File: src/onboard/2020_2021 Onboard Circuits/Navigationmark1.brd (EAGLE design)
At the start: 63.2 x 68.6 mm, 44 parts, among them IC1 A5975D, IC2 A5975D, IC3 CD74AC257M96

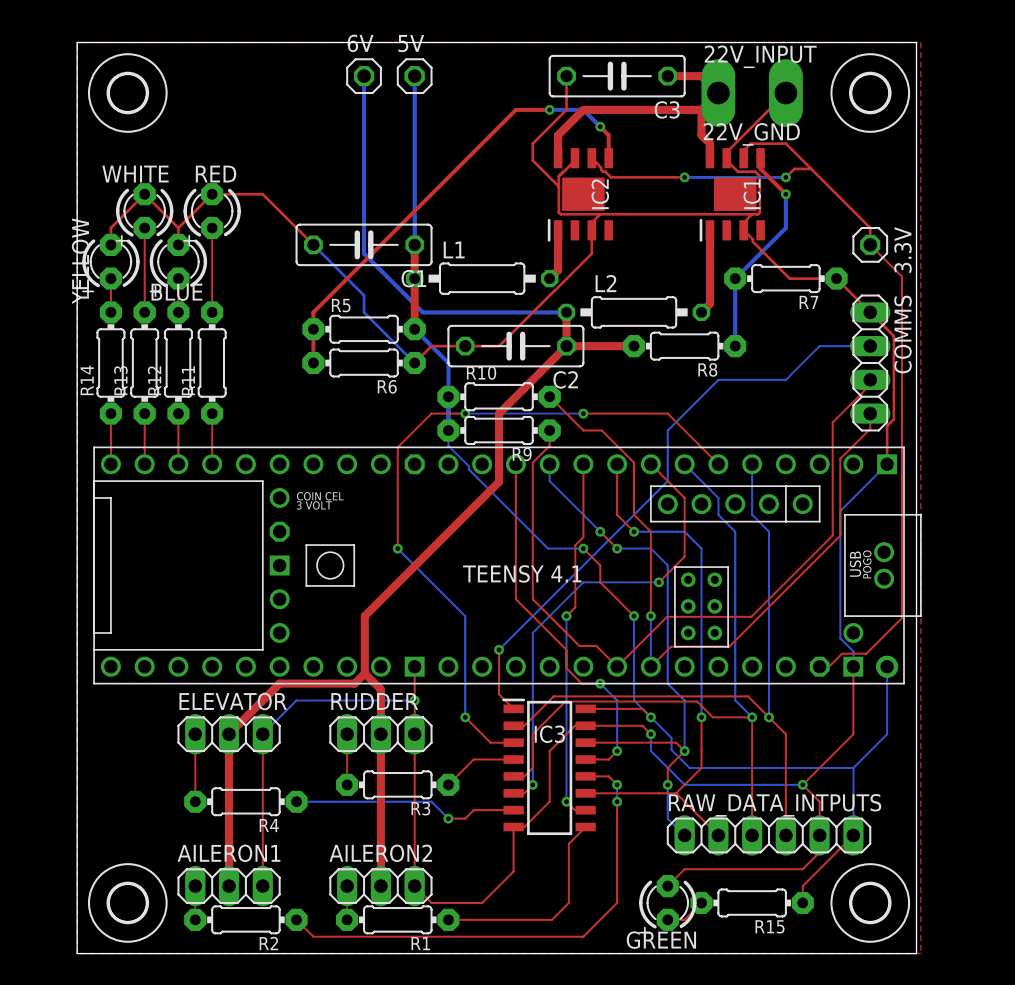
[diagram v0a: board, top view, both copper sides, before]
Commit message: Rounded corners of navigation board. Made corner radius same on both boards.
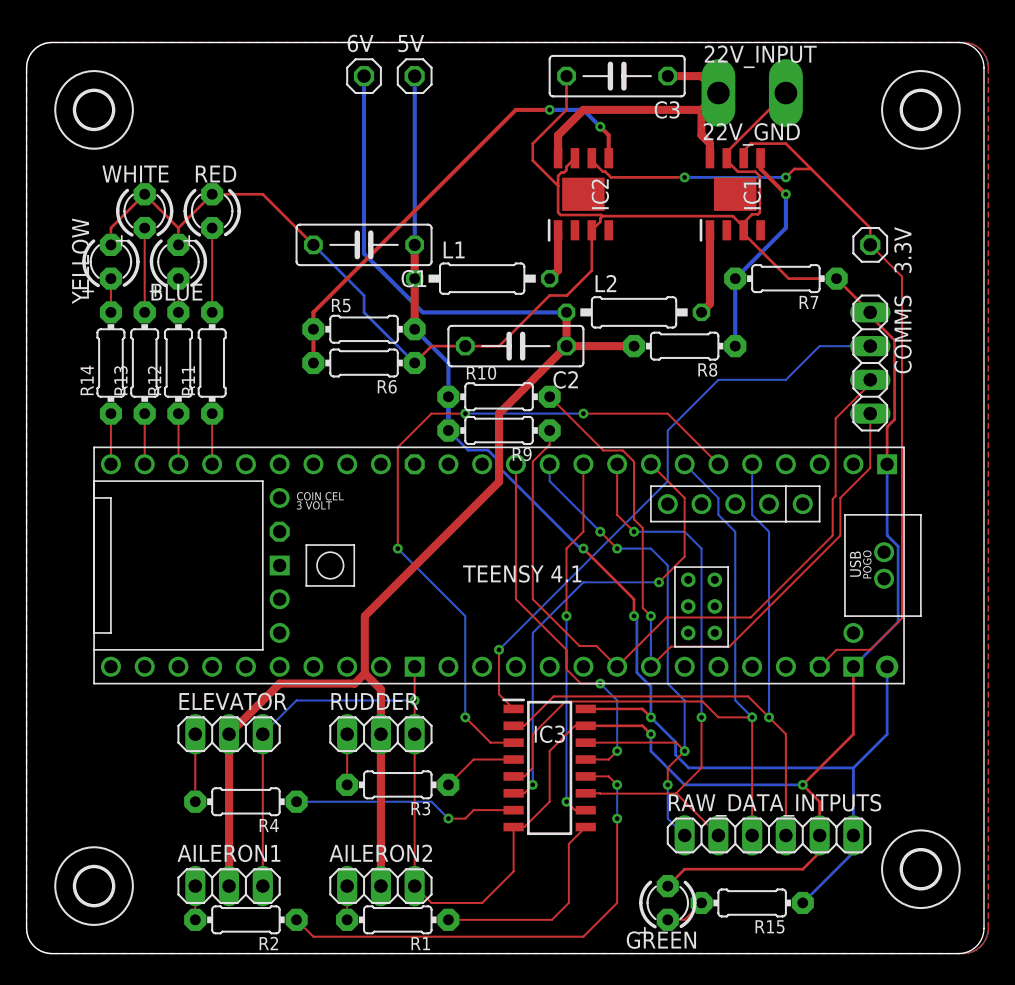
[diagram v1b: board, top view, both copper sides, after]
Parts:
- moved U$2 4.58 mm to (100.3, 16.5)
- moved U$5 4.02 mm to (100.3, 73.7)
- moved U$4 2.84 mm to (38.1, 73.7)
- moved U$3 2.84 mm to (38.1, 15.2)
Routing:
- net GND: track 258.9 -> 252.4 mm
- net 22V: track 24.2 -> 23.4 mm
- net 5V: track 102.6 -> 102.1 mm
- added copper zone on layer 16, net 5V
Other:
- board size 63.2 x 68.6 mm -> 72.1 x 68.6 mm
